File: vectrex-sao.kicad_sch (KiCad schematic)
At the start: 101 parts, among them J1 ICSP, J2 SAO_v169bis, Q1 MMBT3904, U1 PIC16F886-IP, U2 IS31FL3731-SALS2, U3 TC233A

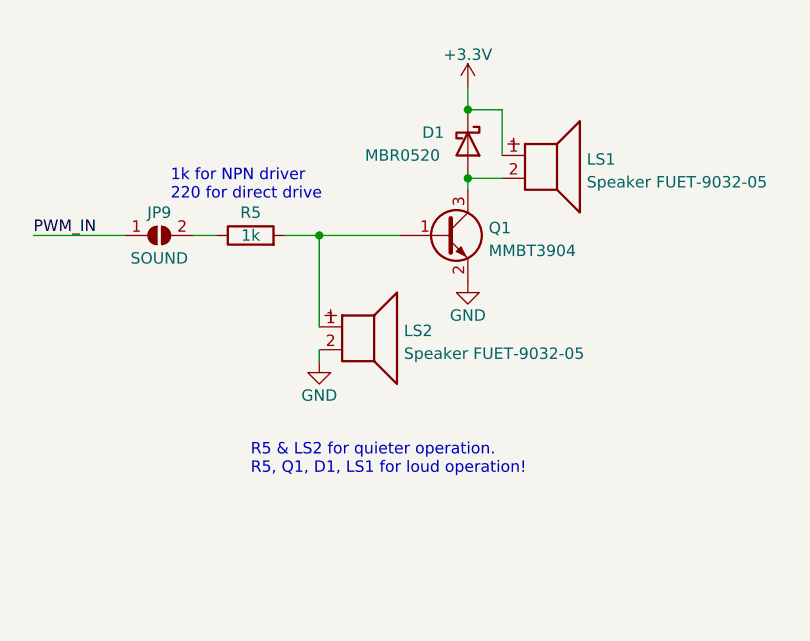
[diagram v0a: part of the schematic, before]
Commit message: update files for easier mass production with JLCPCB
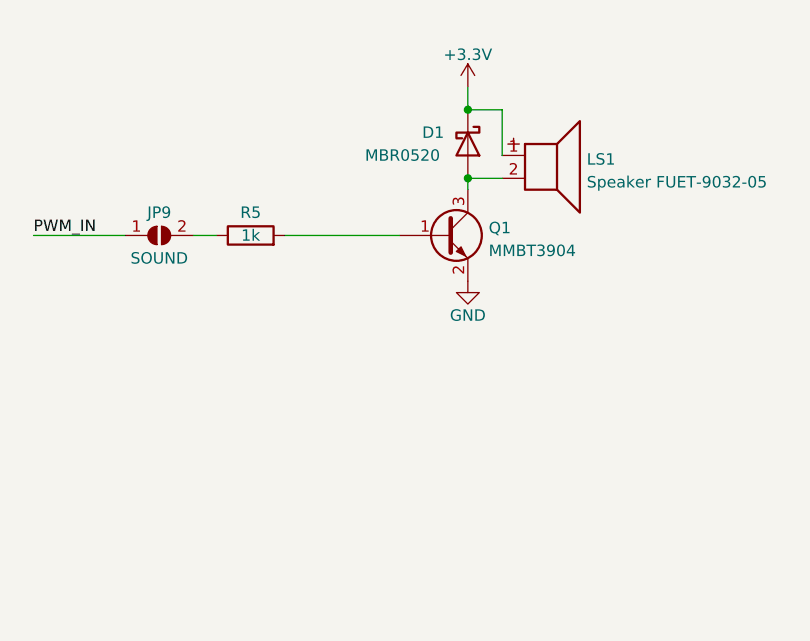
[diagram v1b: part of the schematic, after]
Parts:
- removed LS2: Speaker FUET-9032-05, vectrex-sao:MagneticBuzzer_FUET-9032-05, symbol Device:Speaker
- JP9: footprint vectrex-sao:SolderJumper-2_P1.3mm_Open_RoundedPad1.0x1.5mm -> vectrex-sao:SolderJumper-2_P1.3mm_Bridged_RoundedPad1.0x1.5mm
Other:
- note removed: "1k for NPN driver 220 for direct drive"
- note removed: "R5 & LS2 for quieter operation. R5, Q1, D1, LS1 for loud operation!"
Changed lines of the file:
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@@
 	(title_block
 		(title "Vectrex SAO by Brett Walach")
-		(date "2022-09-24")
-		(rev "v1.0")
+		(date "2025-01-16")
+		(rev "v1.1")
 		(company "https://www.PlayVectrex.com")
-		(comment 1 "@Technobly / Supercon `22")
+		(comment 1 "@Technobly / Supercon `25")
 	)
 	(junction
@@
 	)
 	(junction
-		(at 85.09 200.66)
-		(diameter 0)
-		(color 0 0 0 0)
-	)
-	(junction
 		(at 251.46 110.49)
 		(diameter 0)
@@
 	(wire
 		(pts
-			(xy 81.28 200.66) (xy 85.09 200.66)
-		)
-		(stroke
-			(width 0)
-			(type default)
-		)
-	)
-	(wire
-		(pts
 			(xy 292.1 143.51) (xy 294.64 143.51)
 		)
@@
 	(wire
 		(pts
-			(xy 85.09 200.66) (xy 93.98 200.66)
+			(xy 81.28 200.66) (xy 93.98 200.66)
 		)
 		(stroke
@@
 	(wire
 		(pts
-			(xy 85.09 200.66) (xy 85.09 210.82)
-		)
-		(stroke
-			(width 0)
-			(type default)
-		)
-	)
-	(wire
-		(pts
 			(xy 246.38 34.29) (xy 251.46 34.29)
 		)
@@
 	(wire
 		(pts
-			(xy 85.09 214.63) (xy 85.09 213.36)
-		)
-		(stroke
-			(width 0)
-			(type default)
-		)
-	)
-	(wire
-		(pts
 			(xy 251.46 161.29) (xy 241.3 161.29)
 		)
@@
 		)
 	)
-	(text "1k for NPN driver\n220 for direct drive"
-		(exclude_from_sim no)
-		(at 68.58 196.85 0)
-		(effects
-			(font
-				(size 1.27 1.27)
-			)
-			(justify left bottom)
-		)
-	)
 	(text "Who's in charge??\n  PIC or BADGE"
 		(exclude_from_sim no)
@@
 		)
 	)
-	(text "R5 & LS2 for quieter operation.\nR5, Q1, D1, LS1 for loud operation!"
-		(exclude_from_sim no)
-		(at 77.47 227.33 0)
-		(effects
-			(font
-				(size 1.27 1.27)
-			)
-			(justify left bottom)
-		)
-	)
 	(text "A jumper is installed\nto connect the joystick\nPCB to the TOUCH_PAD\ninput."
 		(exclude_from_sim no)
@@
 			)
 		)
-		(property "Footprint" "vectrex-sao:SolderJumper-2_P1.3mm_Open_RoundedPad1.0x1.5mm"
+		(property "Footprint" "vectrex-sao:SolderJumper-2_P1.3mm_Bridged_RoundedPad1.0x1.5mm"
 			(at 67.31 200.66 0)
 			(effects
@@
 	)
 	(symbol
-		(lib_id "power:GND")
-		(at 85.09 214.63 0)
-		(unit 1)
-		(exclude_from_sim no)
-		(in_bom yes)
-		(on_board yes)
-		(dnp no)
-		(property "Reference" "#PWR0125"
-			(at 85.09 220.98 0)
-			(effects
-				(font
-					(size 1.27 1.27)
-				)
-				(hide yes)
-			)
-		)
-		(property "Value" "GND"
-			(at 85.09 218.44 0)
-			(effects
-				(font
-					(size 1.27 1.27)
-				)
-			)
-		)
-		(property "Footprint" ""
-			(at 85.09 214.63 0)
-			(effects
-				(font
-					(size 1.27 1.27)
-				)
-				(hide yes)
-			)
-		)
-		(property "Datasheet" ""
-			(at 85.09 214.63 0)
-			(effects
-				(font
-					(size 1.27 1.27)
-				)
-				(hide yes)
-			)
-		)
-		(property "Description" ""
-			(at 85.09 214.63 0)
-			(effects
-				(font
-					(size 1.27 1.27)
-				)
-				(hide yes)
-			)
-		)
-		(pin "1"
-		)
-		(instances
-			(project ""
-				(path "/5bd48589-aaed-4c88-bda0-0bb74259d49c"
-					(reference "#PWR0125")
-					(unit 1)
-				)
-			)
-		)
-	)
-	(symbol
 		(lib_id "vectrex-sao:RESISTOR_4PACK")
 		(at 220.98 71.12 270)
@@
 				)
 			)
-		)
-	)
-	(symbol
-		(lib_id "Device:Speaker")
-		(at 90.17 210.82 0)
-		(unit 1)
-		(exclude_from_sim no)
-		(in_bom yes)
-		(on_board yes)
-		(dnp no)
-		(fields_autoplaced yes)
-		(property "Reference" "LS2"
-			(at 94.488 211.2553 0)
-			(effects
-				(font
-					(size 1.27 1.27)
-				)
-				(justify left)
-			)
-		)
-		(property "Value" "Speaker FUET-9032-05"
-			(at 94.488 213.7922 0)
-			(effects
-				(font
-					(size 1.27 1.27)
-				)
-				(justify left)
-			)
-		)
-		(property "Footprint" "vectrex-sao:MagneticBuzzer_FUET-9032-05"
-			(at 90.17 215.9 0)
-			(effects
-				(font
-					(size 1.27 1.27)
-				)
-				(hide yes)
-			)
-		)
-		(property "Datasheet" "~"
-			(at 89.916 212.09 0)
-			(effects
-				(font
-					(size 1.27 1.27)
-				)
-				(hide yes)
-			)
-		)
-		(property "Description" ""
-			(at 90.17 210.82 0)
-			(effects
-				(font
-					(size 1.27 1.27)
-				)
-				(hide yes)
-			)
-		)
-		(pin "1"
-		)
-		(pin "2"
-		)
-		(instances
-			(project ""
-				(path "/5bd48589-aaed-4c88-bda0-0bb74259d49c"
-					(reference "LS2")
-					(unit 1)
-				)
-			)
